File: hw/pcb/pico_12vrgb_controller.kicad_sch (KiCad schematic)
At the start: 19 parts, among them J1 Conn_01x04_RGB, J2 Conn_01x04_RGB, J3 Conn_01x04_RGB, J4 Conn_01x04_RGB, J5 Sata_15pin_Power, Q1 DMG2302U, Q10 DMG2302U, Q11 DMG2302U, Q12 DMG2302U, Q2 DMG2302U, Q3 DMG2302U, Q4 DMG2302U, Q5 DMG2302U, Q6 DMG2302U, Q7 DMG2302U, Q8 DMG2302U, Q9 DMG2302U, U1 Raspberry_Pi_Pico, U2 LM4040C30FTA

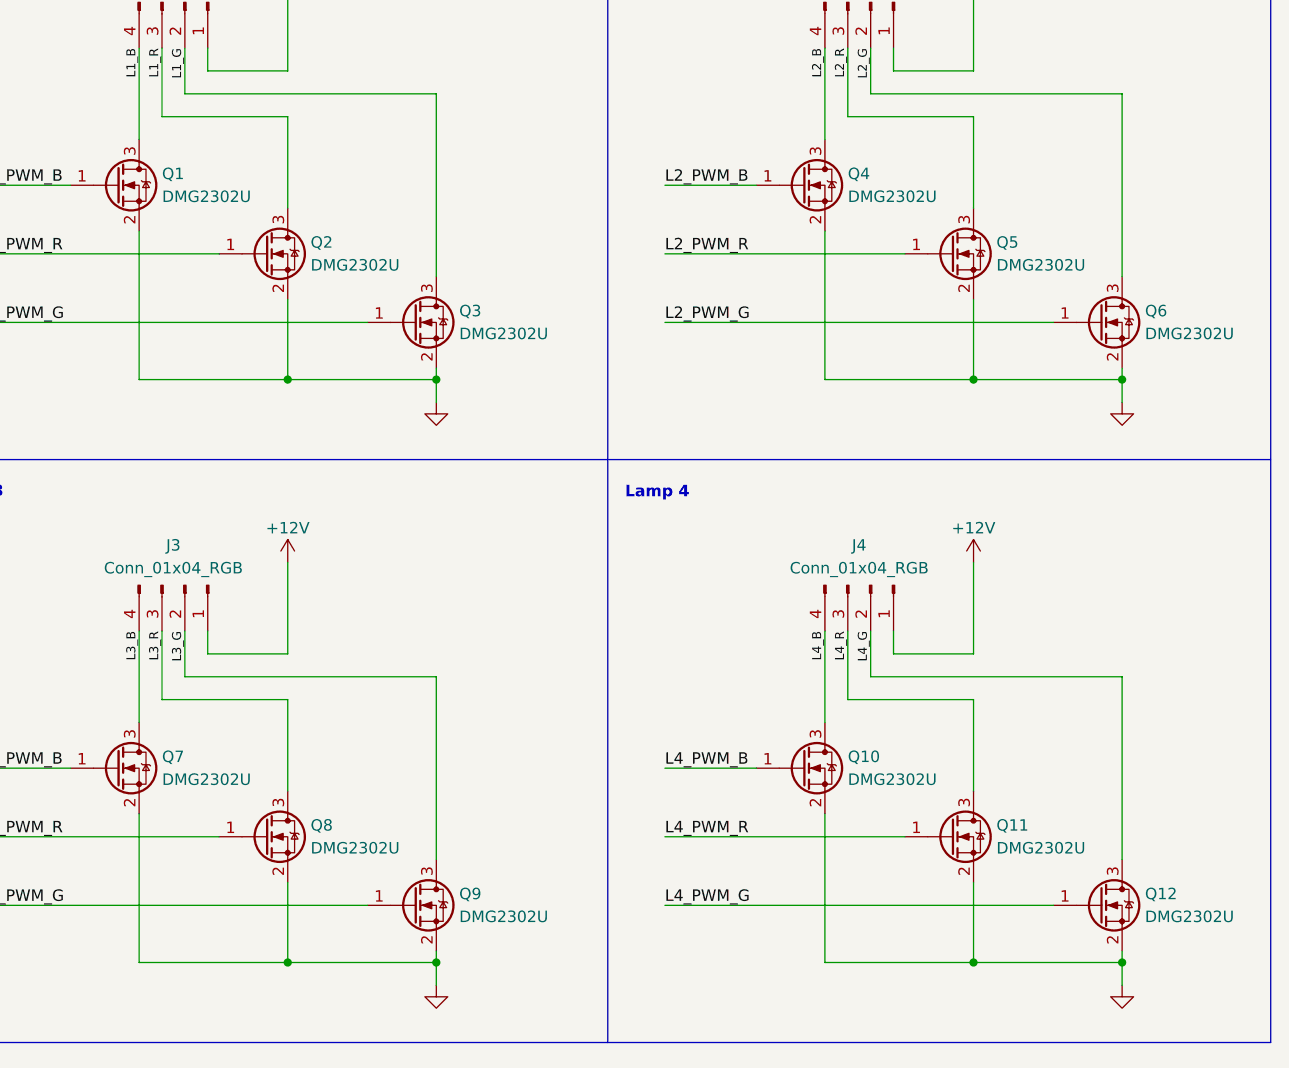
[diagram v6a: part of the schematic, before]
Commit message: Add missing silkscreen markings
Change debug label, add transistor markings, add version number.
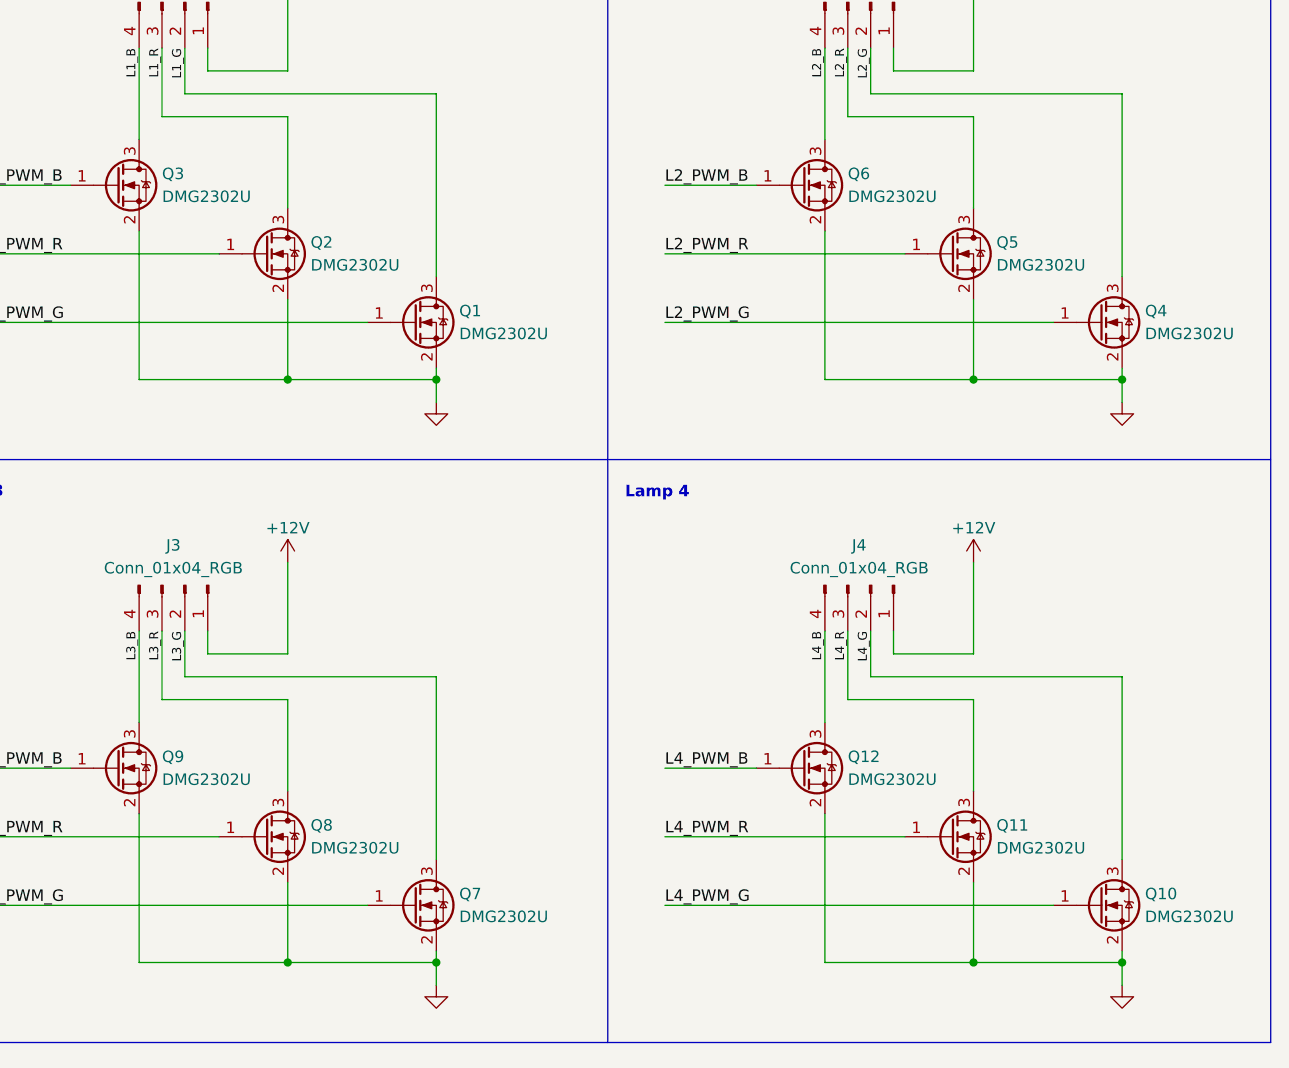
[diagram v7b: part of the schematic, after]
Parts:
- renumbered Q3 to Q1, Q12 to Q10, Q10 to Q12, Q1 to Q3, Q6 to Q4, Q4 to Q6, Q9 to Q7, Q7 to Q9
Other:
- company: BlueKeyes -> bluekeyes
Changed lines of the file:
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@@
     (title "Pico 12VRGB Controller")
     (date "2023-01-17")
-    (rev "0.1")
-    (company "BlueKeyes")
+    (rev "v1")
+    (company "bluekeyes")
     (comment 1 "https://github.com/bluekeyes/pico-12rgb-hid-controller")
   )
@@
   (symbol (lib_id "Transistor_FET:DMG2302U") (at 257.81 138.43 0) (unit 1)
     (in_bom yes) (on_board yes) (dnp no)
-    (property "Reference" "Q12" (at 262.89 137.16 0)
+    (property "Reference" "Q10" (at 262.89 137.16 0)
       (effects (font (size 1.27 1.27)) (justify left))
     )
@@
       (project "pico_12vrgb_controller"
         (path "/8255db78-8f4e-4d30-baf9-cb0573db968b"
-          (reference "Q12") (unit 1)
+          (reference "Q10") (unit 1)
         )
       )
@@
   (symbol (lib_id "Transistor_FET:DMG2302U") (at 148.59 58.42 0) (unit 1)
     (in_bom yes) (on_board yes) (dnp no)
-    (property "Reference" "Q1" (at 153.67 57.15 0)
+    (property "Reference" "Q3" (at 153.67 57.15 0)
       (effects (font (size 1.27 1.27)) (justify left))
     )
@@
       (project "pico_12vrgb_controller"
         (path "/8255db78-8f4e-4d30-baf9-cb0573db968b"
-          (reference "Q1") (unit 1)
+          (reference "Q3") (unit 1)
         )
       )
@@
   (symbol (lib_id "Transistor_FET:DMG2302U") (at 224.79 123.19 0) (unit 1)
     (in_bom yes) (on_board yes) (dnp no)
-    (property "Reference" "Q10" (at 229.87 121.92 0)
+    (property "Reference" "Q12" (at 229.87 121.92 0)
       (effects (font (size 1.27 1.27)) (justify left))
     )
@@
       (project "pico_12vrgb_controller"
         (path "/8255db78-8f4e-4d30-baf9-cb0573db968b"
-          (reference "Q10") (unit 1)
+          (reference "Q12") (unit 1)
         )
       )
@@
   (symbol (lib_id "Transistor_FET:DMG2302U") (at 257.81 73.66 0) (unit 1)
     (in_bom yes) (on_board yes) (dnp no)
-    (property "Reference" "Q6" (at 262.89 72.39 0)
+    (property "Reference" "Q4" (at 262.89 72.39 0)
       (effects (font (size 1.27 1.27)) (justify left))
     )
@@
       (project "pico_12vrgb_controller"
         (path "/8255db78-8f4e-4d30-baf9-cb0573db968b"
-          (reference "Q6") (unit 1)
+          (reference "Q4") (unit 1)
         )
       )
@@
   (symbol (lib_id "Transistor_FET:DMG2302U") (at 181.61 73.66 0) (unit 1)
     (in_bom yes) (on_board yes) (dnp no)
-    (property "Reference" "Q3" (at 186.69 72.39 0)
+    (property "Reference" "Q1" (at 186.69 72.39 0)
       (effects (font (size 1.27 1.27)) (justify left))
     )
@@
       (project "pico_12vrgb_controller"
         (path "/8255db78-8f4e-4d30-baf9-cb0573db968b"
-          (reference "Q3") (unit 1)
+          (reference "Q1") (unit 1)
         )
       )
@@
   (symbol (lib_id "Transistor_FET:DMG2302U") (at 148.59 123.19 0) (unit 1)
     (in_bom yes) (on_board yes) (dnp no)
-    (property "Reference" "Q7" (at 153.67 121.92 0)
+    (property "Reference" "Q9" (at 153.67 121.92 0)
       (effects (font (size 1.27 1.27)) (justify left))
     )
@@
       (project "pico_12vrgb_controller"
         (path "/8255db78-8f4e-4d30-baf9-cb0573db968b"
-          (reference "Q7") (unit 1)
+          (reference "Q9") (unit 1)
         )
       )
@@
   (symbol (lib_id "Transistor_FET:DMG2302U") (at 181.61 138.43 0) (unit 1)
     (in_bom yes) (on_board yes) (dnp no)
-    (property "Reference" "Q9" (at 186.69 137.16 0)
+    (property "Reference" "Q7" (at 186.69 137.16 0)
       (effects (font (size 1.27 1.27)) (justify left))
     )
@@
       (project "pico_12vrgb_controller"
         (path "/8255db78-8f4e-4d30-baf9-cb0573db968b"
-          (reference "Q9") (unit 1)
+          (reference "Q7") (unit 1)
         )
       )
@@
   (symbol (lib_id "Transistor_FET:DMG2302U") (at 224.79 58.42 0) (unit 1)
     (in_bom yes) (on_board yes) (dnp no)
-    (property "Reference" "Q4" (at 229.87 57.15 0)
+    (property "Reference" "Q6" (at 229.87 57.15 0)
       (effects (font (size 1.27 1.27)) (justify left))
     )
@@
       (project "pico_12vrgb_controller"
         (path "/8255db78-8f4e-4d30-baf9-cb0573db968b"
-          (reference "Q4") (unit 1)
-        )
-      )
+          (reference "Q6") (unit 1)
+        )
+      )
